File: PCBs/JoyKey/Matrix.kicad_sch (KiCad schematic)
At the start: 20 parts, among them SW11 SW_Push_45deg, SW12 SW_Push_45deg, SW2 SW_Push_45deg, SW3 SW_Push_45deg, SW4 SW_Push_45deg, SW5 SW_Push_45deg, SW6 SW_Push_45deg, SW7 SW_Push_45deg

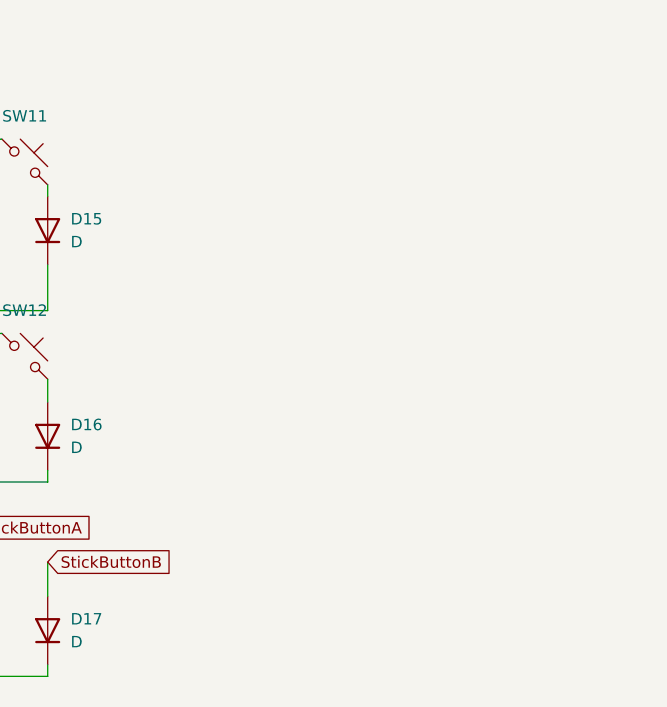
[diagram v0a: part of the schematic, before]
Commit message: Add draft schematics for all the input sources
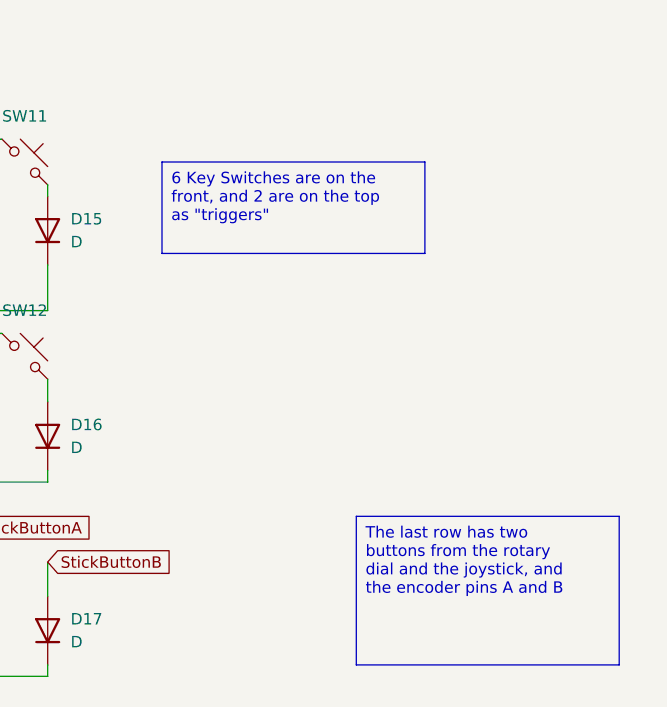
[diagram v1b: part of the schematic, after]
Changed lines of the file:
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@@
+		)
+	)
+	(text_box "6 Key Switches are on the front, and 2 are on the top as \"triggers\""
+		(exclude_from_sim no)
+		(at 134.62 49.53 0)
+		(size 29.21 10.16)
+		(stroke
+			(width 0)
+			(type default)
+		)
+		(fill
+			(type none)
+		)
+		(effects
+			(font
+				(size 1.27 1.27)
+			)
+			(justify left top)
+		)
+	)
+	(text_box "The last row has two buttons from the rotary dial and the joystick, and the encoder pins A and B"
+		(exclude_from_sim no)
+		(at 156.21 88.9 0)
+		(size 29.21 16.51)
+		(stroke
+			(width 0)
+			(type default)
+		)
+		(fill
+			(type none)
+		)
+		(effects
+			(font
+				(size 1.27 1.27)
+			)
+			(justify left top)
 		)
 	)

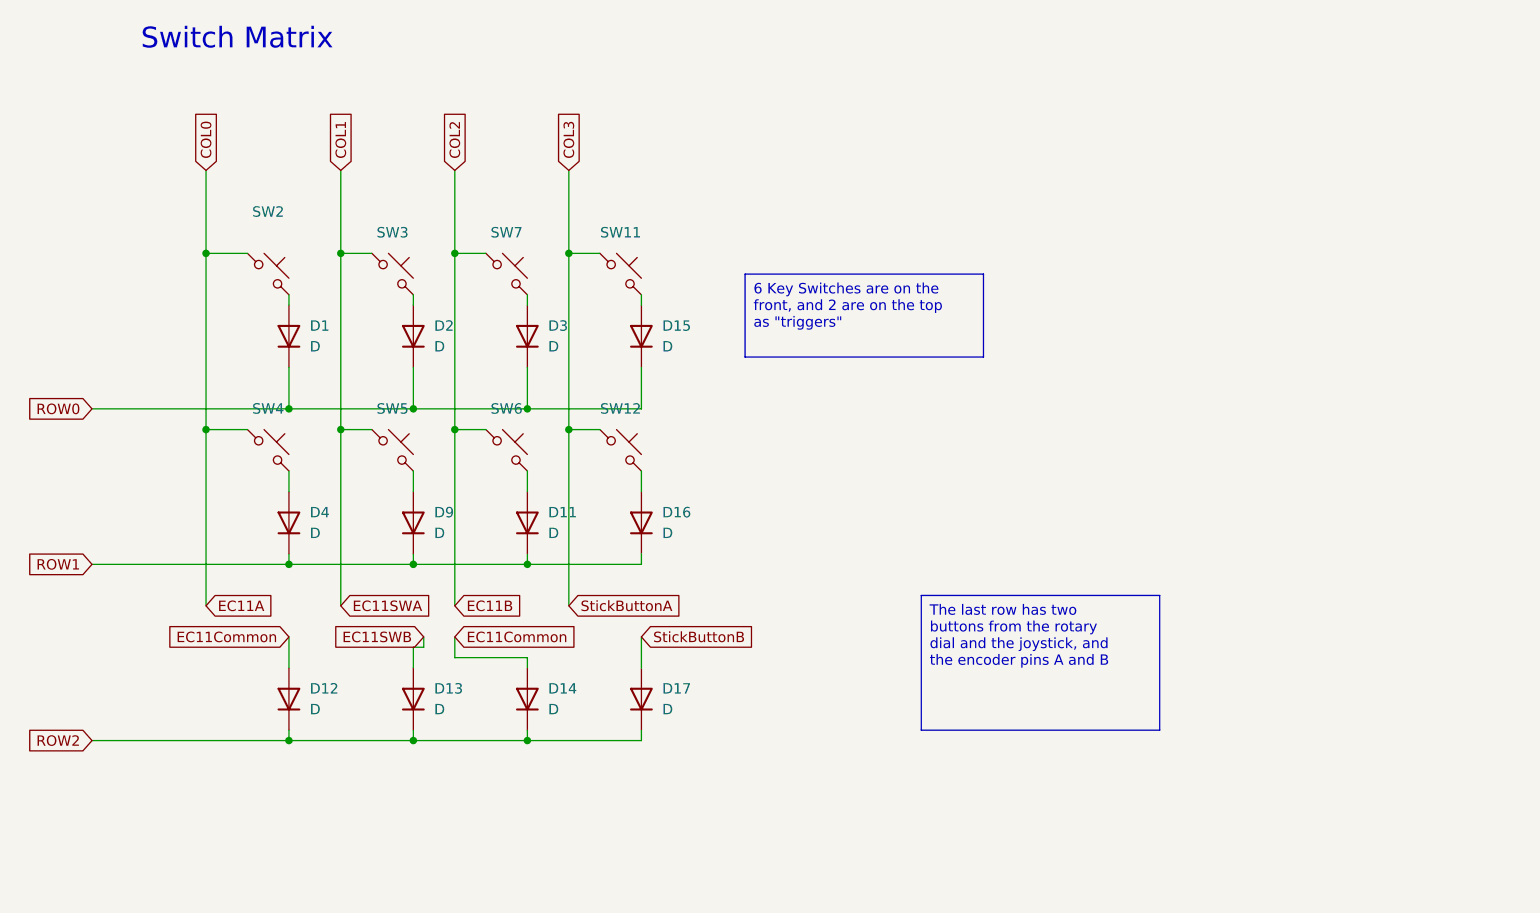
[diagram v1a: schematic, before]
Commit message: Updated matrix for encoder
I swapped the common pin on the encoder to be connected to the columns since my scanning will be col2row. I don't want the common to go through two diodes!
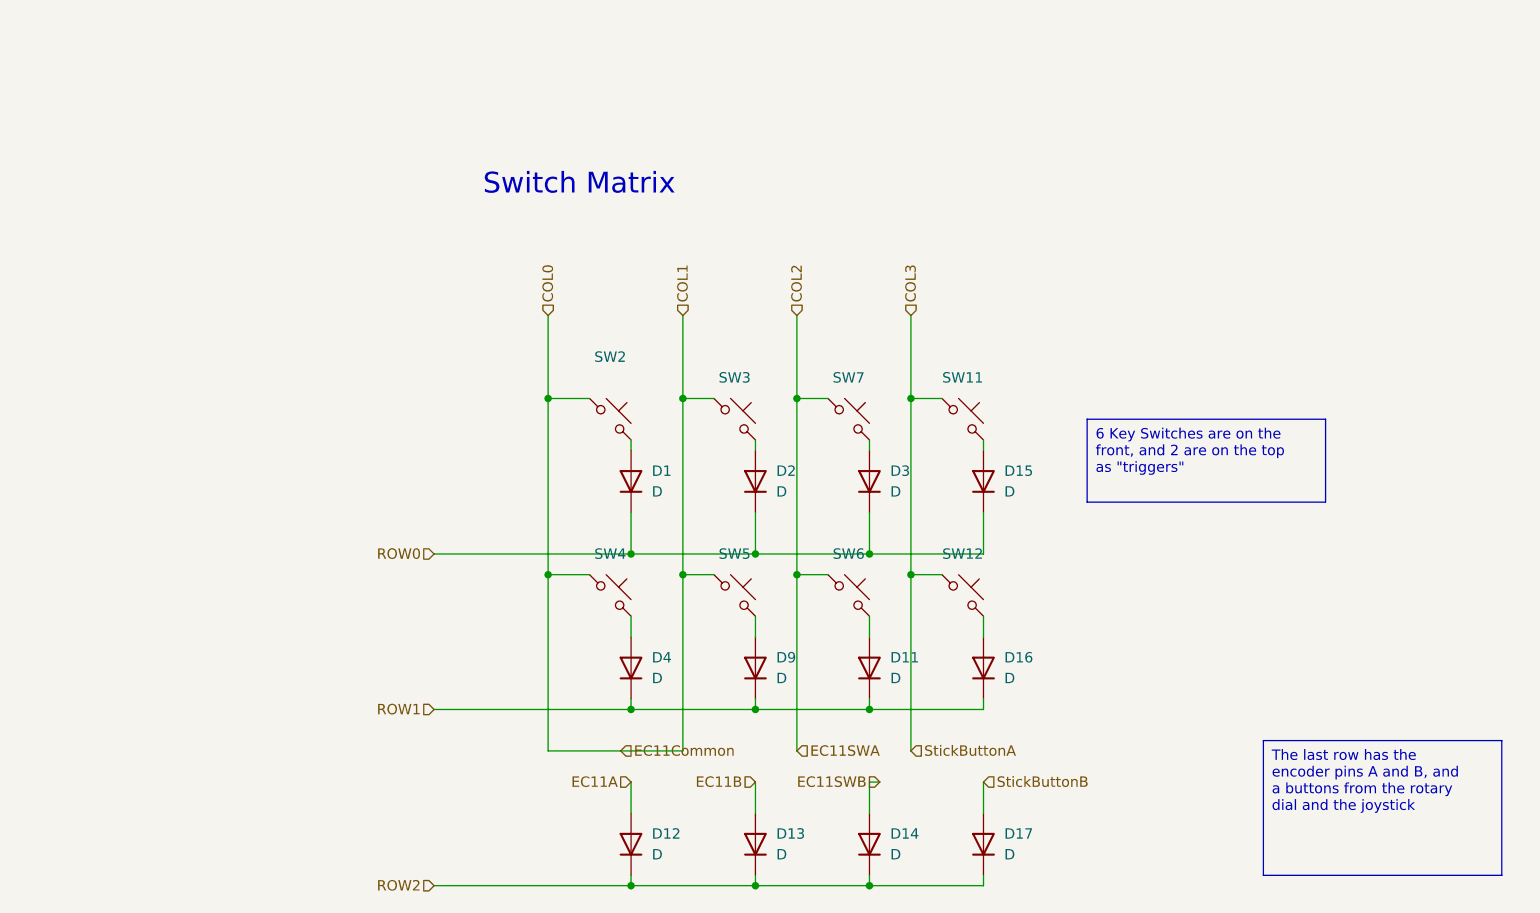
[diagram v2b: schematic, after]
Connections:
- net COL1 is gone; now on net COL0: SW3.1, SW5.1
- net EC11SWB: now also D14.2 (A); no longer D13.2 (A)
- net EC11Common renamed EC11A
- net EC11A: no longer D14.2 (A)
- new net EC11B: D13.2 (A)
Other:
- moved on the sheet: D1, D11, D12, D13, D14, D15, D16, D17, D2, D3, D4, D9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

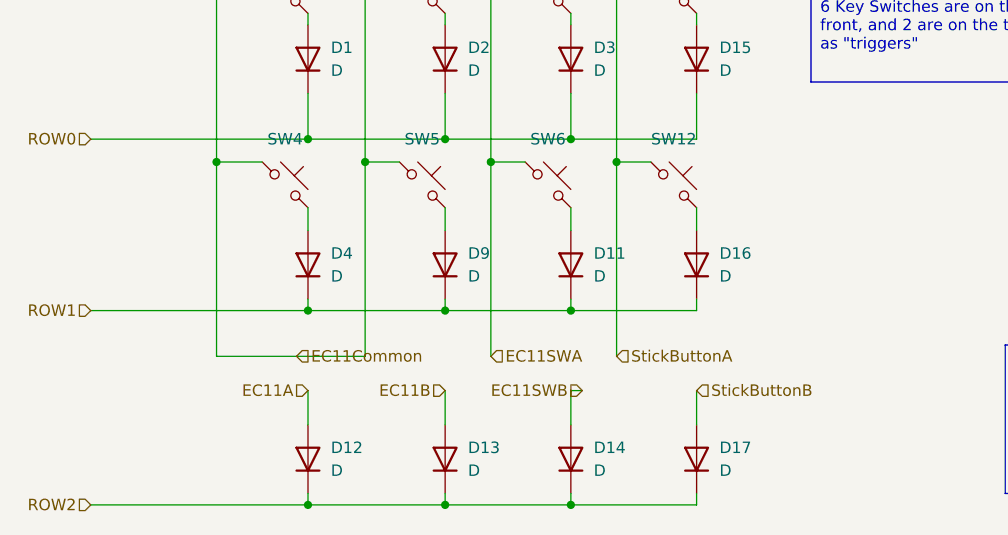
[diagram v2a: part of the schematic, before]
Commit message: Added netties to matrix for encoder inputs
I want the nets to be separate in different areas, so I have added netties
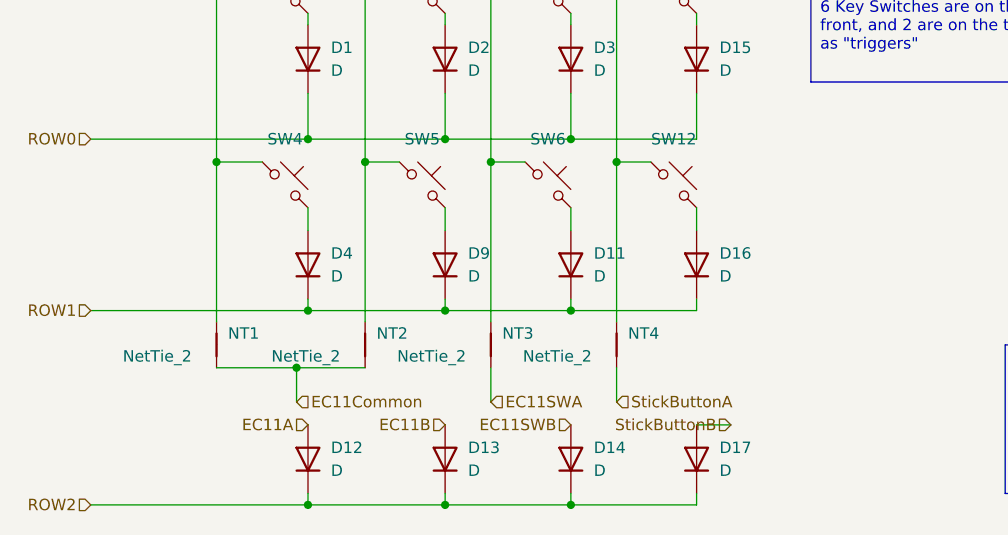
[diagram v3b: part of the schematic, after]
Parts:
- added NT1, NT2, NT3, NT4: NetTie_2, custom_Connector:NetTie-2_SMD_Pad0.2mm, symbol Device:NetTie_2
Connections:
- net COL0: now also NT1.2; no longer SW3.1, SW5.1
- net COL2: now also NT3.2
- net COL3: now also NT4.2
- new net COL1: NT2.2, SW3.1, SW5.1
- new net EC11Common: NT1.1, NT2.1
- new net EC11SWA: NT3.1
- new net StickButtonA: NT4.1

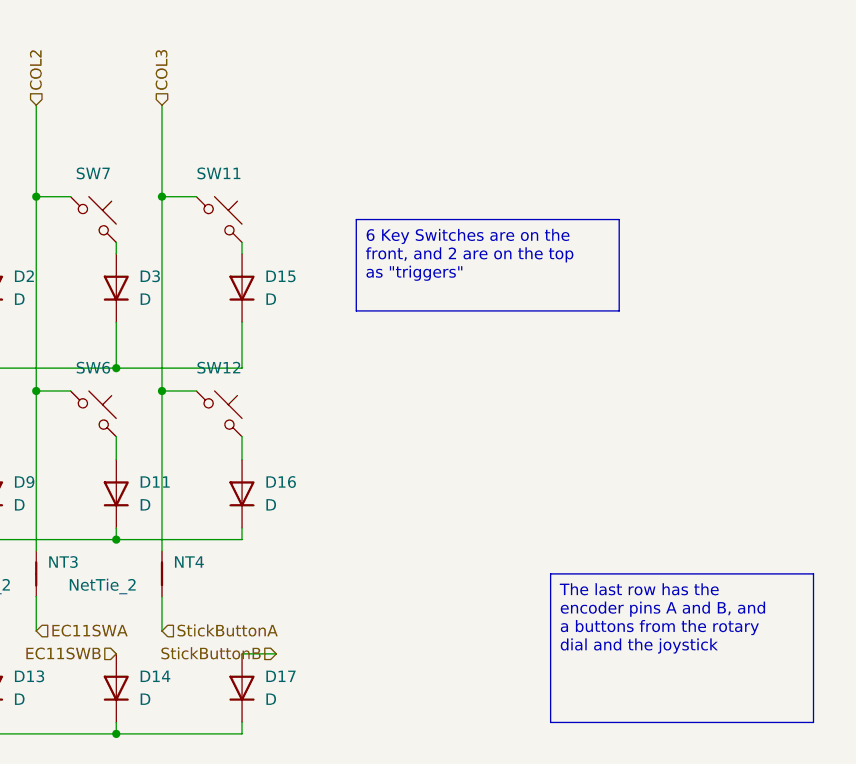
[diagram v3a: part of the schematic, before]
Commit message: Replaced 2 keys with headers for top Triggers
Since there are not right angle keys (just buttons), I will use normal keys embedded in the case with wires soldering to the board
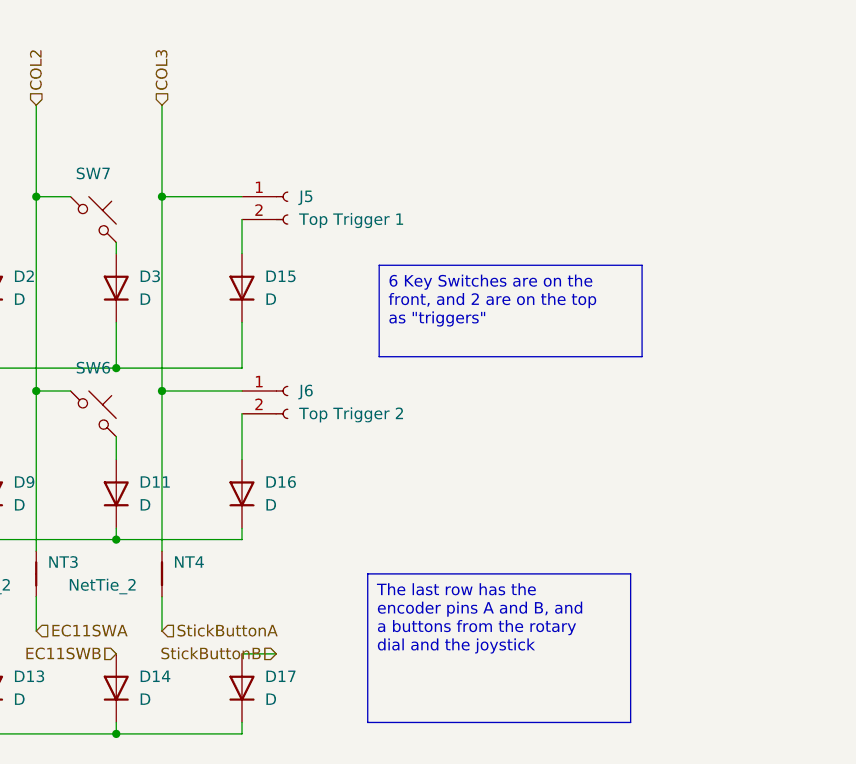
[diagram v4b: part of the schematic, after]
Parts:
- removed SW11, SW12: SW_Push_45deg, MX_Solderable:MX-Solderable-1U, symbol Switch:SW_Push_45deg
- added J5: Top Trigger 1, Connector_PinHeader_2.54mm:PinHeader_1x02_P2.54mm_Vertical, symbol Connector:Conn_01x02_Socket
- added J6: Top Trigger 2, Connector_PinHeader_2.54mm:PinHeader_1x02_P2.54mm_Vertical, symbol Connector:Conn_01x02_Socket
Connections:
- net COL3: now also J5.1 (Pin_1), J6.1 (Pin_1)
- net at D16.2 (A): now also J6.2 (Pin_2)
- net at D15.2 (A): now also J5.2 (Pin_2)
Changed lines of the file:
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@@
 	(wire
 		(pts
-			(xy 154.94 86.36) (xy 158.75 86.36)
+			(xy 154.94 86.36) (xy 163.83 86.36)
 		)
 		(stroke
@@
 	(wire
 		(pts
-			(xy 163.83 91.44) (xy 163.83 93.98)
-		)
-		(stroke
-			(width 0)
-			(type default)
-		)
-	)
-	(wire
-		(pts
 			(xy 154.94 64.77) (xy 154.94 86.36)
 		)
@@
 	(wire
 		(pts
-			(xy 163.83 69.85) (xy 163.83 71.12)
+			(xy 163.83 67.31) (xy 163.83 71.12)
 		)
 		(stroke
@@
 	(wire
 		(pts
+			(xy 163.83 88.9) (xy 163.83 93.98)
+		)
+		(stroke
+			(width 0)
+			(type default)
+		)
+	)
+	(wire
+		(pts
 			(xy 120.65 102.87) (xy 135.89 102.87)
 		)
@@
 	(wire
 		(pts
-			(xy 154.94 64.77) (xy 158.75 64.77)
+			(xy 154.94 64.77) (xy 163.83 64.77)
 		)
 		(stroke
@@
 	(text_box "6 Key Switches are on the front, and 2 are on the top as \"triggers\""
 		(exclude_from_sim no)
-		(at 176.53 67.31 0)
+		(at 179.07 72.39 0)
 		(size 29.21 10.16)
 		(stroke
@@
 	(text_box "The last row has the encoder pins A and B, and a buttons from the rotary dial and the joystick "
 		(exclude_from_sim no)
-		(at 198.12 106.68 0)
+		(at 177.8 106.68 0)
 		(size 29.21 16.51)
 		(stroke
@@
 	)
 	(symbol
+		(lib_id "Connector:Conn_01x02_Socket")
+		(at 168.91 86.36 0)
+		(unit 1)
+		(exclude_from_sim no)
+		(in_bom yes)
+		(on_board yes)
+		(dnp no)
+		(fields_autoplaced yes)
+		(property "Reference" "J6"
+			(at 170.18 86.3599 0)
+			(effects
+				(font
+					(size 1.27 1.27)
+				)
+				(justify left)
+			)
+		)
+		(property "Value" "Top Trigger 2"
+			(at 170.18 88.8999 0)
+			(effects
+				(font
+					(size 1.27 1.27)
+				)
+				(justify left)
+			)
+		)
+		(property "Footprint" "Connector_PinHeader_2.54mm:PinHeader_1x02_P2.54mm_Vertical"
+			(at 168.91 86.36 0)
+			(effects
+				(font
+					(size 1.27 1.27)
+				)
+				(hide yes)
+			)
+		)
+		(property "Datasheet" "~"
+			(at 168.91 86.36 0)
+			(effects
+				(font
+					(size 1.27 1.27)
+				)
+				(hide yes)
+			)
+		)
+		(property "Description" "Generic connector, single row, 01x02, script generated"
+			(at 168.91 86.36 0)
+			(effects
+				(font
+					(size 1.27 1.27)
+				)
+				(hide yes)
+			)
+		)
+		(pin "2"
+		)
+		(pin "1"
+		)
+		(instances
+			(project "JoyKey"
+				(path "/7995ec7a-c14b-437e-b354-3eb74052b7cb/68ef131f-9d28-47fd-9e2d-054e6cdf50c5"
+					(reference "J6")
+					(unit 1)
+				)
+			)
+		)
+	)
+	(symbol
 		(lib_id "Device:D")
 		(at 149.86 119.38 90)
@@
 	(symbol
 		(lib_id "Switch:SW_Push_45deg")
-		(at 161.29 88.9 0)
-		(unit 1)
-		(exclude_from_sim no)
-		(in_bom yes)
-		(on_board yes)
-		(dnp no)
-		(fields_autoplaced yes)
-		(property "Reference" "SW12"
-			(at 161.29 83.82 0)
-			(effects
-				(font
-					(size 1.27 1.27)
-				)
-			)
-		)
-		(property "Value" "SW_Push_45deg"
-			(at 161.29 83.82 0)
-			(effects
-				(font
-					(size 1.27 1.27)
-				)
-				(hide yes)
-			)
-		)
-		(property "Footprint" "MX_Solderable:MX-Solderable-1U"
-			(at 161.29 88.9 0)
-			(effects
-				(font
-					(size 1.27 1.27)
-				)
-				(hide yes)
-			)
-		)
-		(property "Datasheet" "~"
-			(at 161.29 88.9 0)
-			(effects
-				(font
-					(size 1.27 1.27)
-				)
-				(hide yes)
-			)
-		)
-		(property "Description" "Push button switch, normally open, two pins, 45° tilted"
-			(at 161.29 88.9 0)
-			(effects
-				(font
-					(size 1.27 1.27)
-				)
-				(hide yes)
-			)
-		)
-		(pin "1"
-		)
-		(pin "2"
-		)
-		(instances
-			(project "JoyKey"
-				(path "/7995ec7a-c14b-437e-b354-3eb74052b7cb/68ef131f-9d28-47fd-9e2d-054e6cdf50c5"
-					(reference "SW12")
-					(unit 1)
-				)
-			)
-		)
-	)
-	(symbol
-		(lib_id "Switch:SW_Push_45deg")
 		(at 118.11 67.31 0)
 		(unit 1)
@@
 	)
 	(symbol
-		(lib_id "Switch:SW_Push_45deg")
-		(at 161.29 67.31 0)
+		(lib_id "Connector:Conn_01x02_Socket")
+		(at 168.91 64.77 0)
 		(unit 1)
 		(exclude_from_sim no)
@@
 		(dnp no)
 		(fields_autoplaced yes)
-		(property "Reference" "SW11"
-			(at 161.29 62.23 0)
-			(effects
-				(font
-					(size 1.27 1.27)
-				)
-			)
-		)
-		(property "Value" "SW_Push_45deg"
-			(at 161.29 62.23 0)
-			(effects
-				(font
-					(size 1.27 1.27)
-				)
-				(hide yes)
-			)
-		)
-		(property "Footprint" "MX_Solderable:MX-Solderable-1U"
-			(at 161.29 67.31 0)
+		(property "Reference" "J5"
+			(at 170.18 64.7699 0)
+			(effects
+				(font
+					(size 1.27 1.27)
+				)
+				(justify left)
+			)
+		)
+		(property "Value" "Top Trigger 1"
+			(at 170.18 67.3099 0)
+			(effects
+				(font
+					(size 1.27 1.27)
+				)
+				(justify left)
+			)
+		)
+		(property "Footprint" "Connector_PinHeader_2.54mm:PinHeader_1x02_P2.54mm_Vertical"
+			(at 168.91 64.77 0)
 			(effects
 				(font
@@
 		)
 		(property "Datasheet" "~"
-			(at 161.29 67.31 0)
-			(effects
-				(font
-					(size 1.27 1.27)
-				)
-				(hide yes)
-			)
-		)
-		(property "Description" "Push button switch, normally open, two pins, 45° tilted"
-			(at 161.29 67.31 0)
-			(effects
-				(font
-					(size 1.27 1.27)
-				)
-				(hide yes)
-			)
+			(at 168.91 64.77 0)
+			(effects
+				(font
+					(size 1.27 1.27)
+				)
+				(hide yes)
+			)
+		)
+		(property "Description" "Generic connector, single row, 01x02, script generated"
+			(at 168.91 64.77 0)
+			(effects
+				(font
+					(size 1.27 1.27)
+				)
+				(hide yes)
+			)
+		)
+		(pin "2"
 		)
 		(pin "1"
 		)
-		(pin "2"
-		)
 		(instances
-			(project "JoyKey"
+			(project ""
 				(path "/7995ec7a-c14b-437e-b354-3eb74052b7cb/68ef131f-9d28-47fd-9e2d-054e6cdf50c5"
-					(reference "SW11")
+					(reference "J5")
 					(unit 1)
 				)
